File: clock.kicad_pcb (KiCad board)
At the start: 2 copper layers, 90 x 50 mm, 28 parts, among them J1 Conn_01x04, SW1 SW_Push, SW2 SW_Push_SPDT, U3 74LS32, U4 74LS04, U5 74LS08

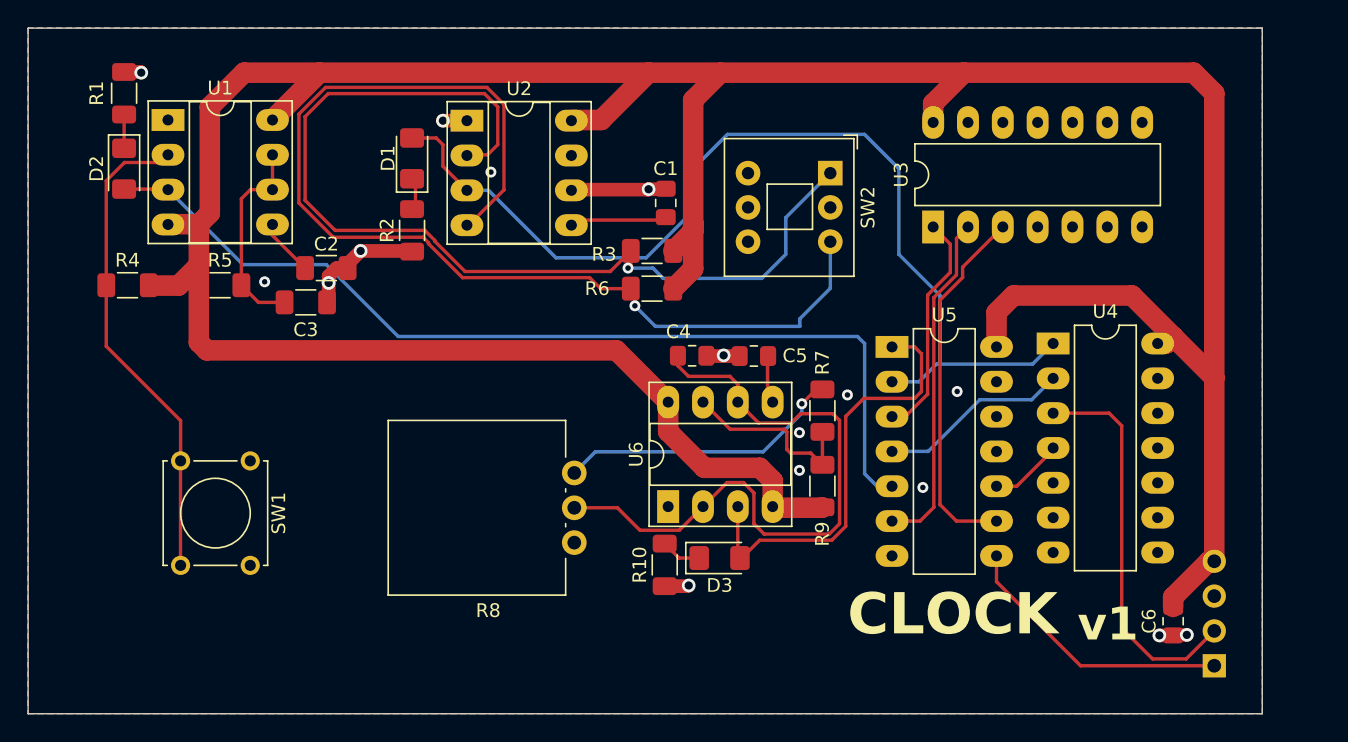
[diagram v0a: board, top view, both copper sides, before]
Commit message: Fix non standard switch buton
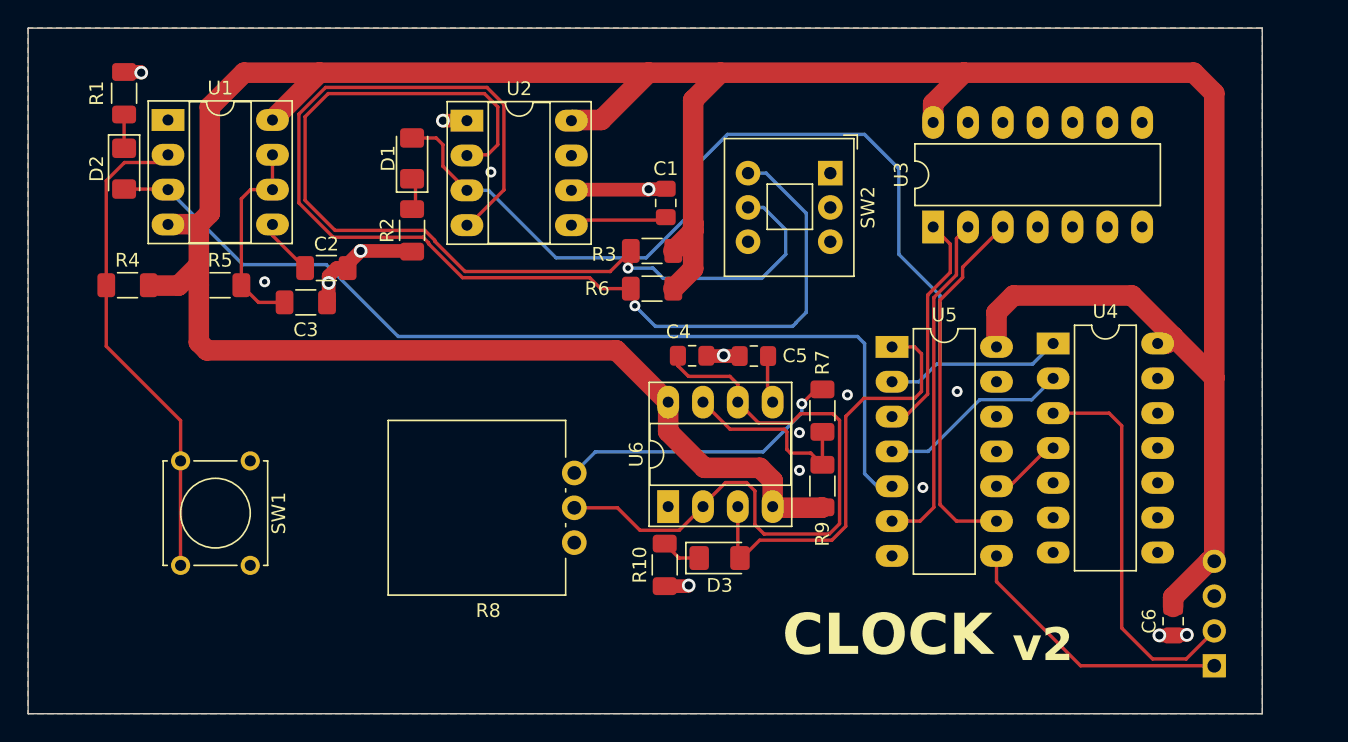
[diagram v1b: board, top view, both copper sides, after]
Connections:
- net /HLT renamed HLT
- SW2 pad 1: Net-(SW2-A) -> (no net)
- SW2 pad 2: GND -> (no net)
- SW2 pad 3: Net-(SW2-C) -> (no net)
- SW2 pad 4: (no net) -> Net-(SW2-C)
- SW2 pad 5: (no net) -> Net-(SW2-A)
- SW2 pad 6: (no net) -> GND
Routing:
- net Net-(SW2-C): track 80.7 -> 87.2 mm
- net Net-(SW2-A): track 74.3 -> 72.2 mm
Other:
- board text added: "CLOCK _{v2}"
- board text removed: "CLOCK _{v1}"
